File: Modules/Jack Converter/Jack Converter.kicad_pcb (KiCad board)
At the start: 2 copper layers, 45 x 175 mm, 27 parts, among them J1 TS_Jack_3.5mm_Sw, J10 TS_Jack_6.35mm_Sw, J100 IDC_02x08, J11 TS_Jack_3.5mm_Sw, J12 TS_Jack_6.35mm_Sw, J13 TS_Jack_3.5mm_Sw, J14 TS_Jack_6.35mm_Sw, J15 TS_Jack_3.5mm_Sw, J16 TS_Jack_6.35mm_Sw, J17 TS_Jack_3.5mm_Sw, J18 TS_Jack_6.35mm_Sw, J2 TS_Jack_6.35mm_Sw, J3 TS_Jack_3.5mm_Sw, J4 TS_Jack_6.35mm_Sw, J5 TS_Jack_3.5mm_Sw, J50 Conn_01x08_BackboneTap, J6 TS_Jack_6.35mm_Sw, J7 TS_Jack_3.5mm_Sw, J8 TS_Jack_6.35mm_Sw, J9 TS_Jack_3.5mm_Sw, SW1 SW_DPDT, SW2 SW_DPDT, SW3 SW_DPDT

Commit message: Positioned components precisely
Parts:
- moved J17 8.94 mm to (72.5, 185.0), turned to 90 degrees
- moved J18 8.54 mm to (89.0, 185.0), turned to 90 degrees
- moved J100 8.51 mm to (53.2, 186.1)
- moved J15 8.06 mm to (72.5, 168.5), turned to 90 degrees
- moved J16 7.51 mm to (89.0, 168.5), turned to 90 degrees
- moved J13 7.21 mm to (72.5, 152.0), turned to 90 degrees
- moved J14 6.74 mm to (89.0, 152.0), turned to 90 degrees
- moved TP4 6.58 mm to (56.0, 152.0)
- moved J11 6.40 mm to (72.5, 135.5), turned to 90 degrees
- moved J50 6.21 mm to (63.6, 215.0)
- moved J9 6.02 mm to (72.5, 119.0), turned to 90 degrees
- moved J12 5.98 mm to (89.0, 135.5), turned to 90 degrees
- moved J10 5.26 mm to (89.0, 119.0), turned to 90 degrees
- moved TP3 5.10 mm to (56.0, 119.0)
- moved SW3 5.08 mm to (54.7, 133.0)
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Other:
- board size 45 x 175 mm -> 48 x 175 mm

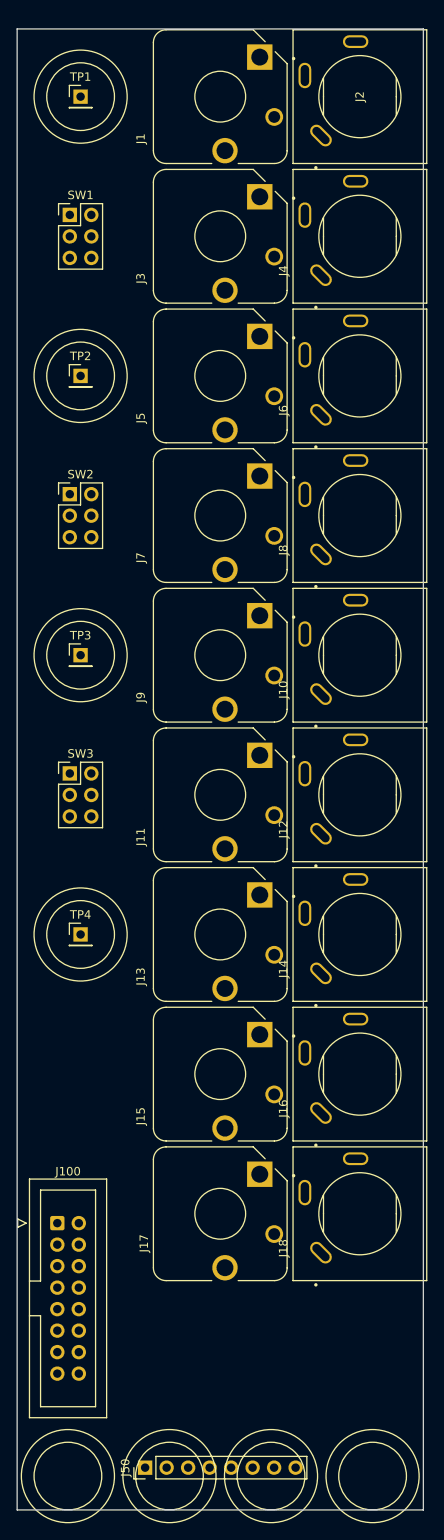
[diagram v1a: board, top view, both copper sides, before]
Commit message: Added extra row of jacks, finished positioning
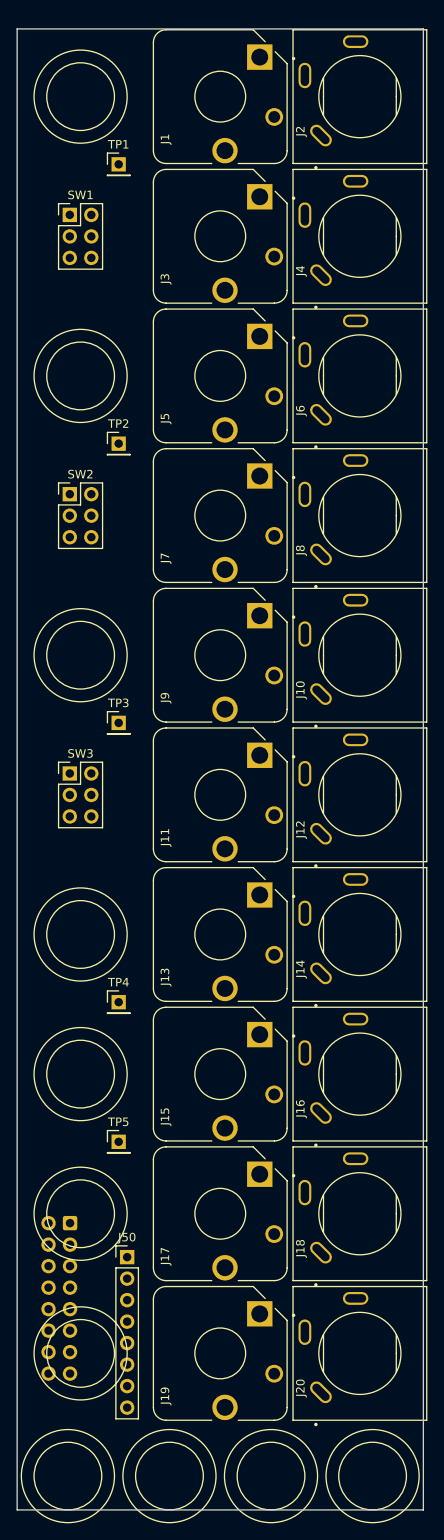
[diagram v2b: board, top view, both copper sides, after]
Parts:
- added J19: TS_Jack_3.5mm_Sw, SynthStuff:AMPHENOL_ACJM-MV35-2S, F.Cu at (72.5, 201.5)
- added J20: TS_Jack_6.35mm_Sw, SynthStuff:CUI_MJ-63052A, F.Cu at (89.0, 201.5)
- added TP5: Banana_Jack, Connector_PinHeader_2.54mm:PinHeader_1x01_P2.54mm_Vertical, F.Cu at (60.5, 176.5)
- J100: moved to B.Cu
- moved J50 25.0 mm to (61.5, 190.1), turned to 0 degrees
- moved TP1 9.18 mm to (60.5, 61.0)
- moved TP2 9.18 mm to (60.5, 94.0)
- moved TP3 9.18 mm to (60.5, 127.0)
- moved TP4 9.18 mm to (60.5, 160.0)
- moved J100 1.50 mm to (54.8, 186.1), turned to 180 degrees
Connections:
- J15 pad T: Net-(J100-Pin_7a) -> Net-(J15-PadT)
- J16 pad T: Net-(J100-Pin_7a) -> Net-(J15-PadT)
- J17 pad T: Net-(J100-Pin_8a) -> Net-(J100-Pin_7a)
- J18 pad T: Net-(J100-Pin_8a) -> Net-(J100-Pin_7a)

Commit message: Routed tracks
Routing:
- net GND: track 0.00 -> 262.3 mm
- net Net-(J10-PadT): track 0.00 -> 82.9 mm
- net Net-(J5-PadT): track 0.00 -> 82.7 mm
- net Net-(J13-PadT): track 0.00 -> 66.2 mm
- net Net-(J1-PadT): track 0.00 -> 51.9 mm
- net Net-(J100-Pin_7a): track 0.00 -> 51.7 mm
- net Net-(J100-Pin_8a): track 0.00 -> 44.5 mm
- net Net-(J11-PadT): track 0.00 -> 40.4 mm
- net Net-(J7-PadT): track 0.00 -> 40.4 mm
- net Net-(J3-PadT): track 0.00 -> 40.4 mm
- net Net-(J15-PadT): track 0.00 -> 35.2 mm
- net -12V: track 0.00 -> 11.0 mm
- net +5V: track 0.00 -> 11.0 mm
- net +12V: track 0.00 -> 11.0 mm

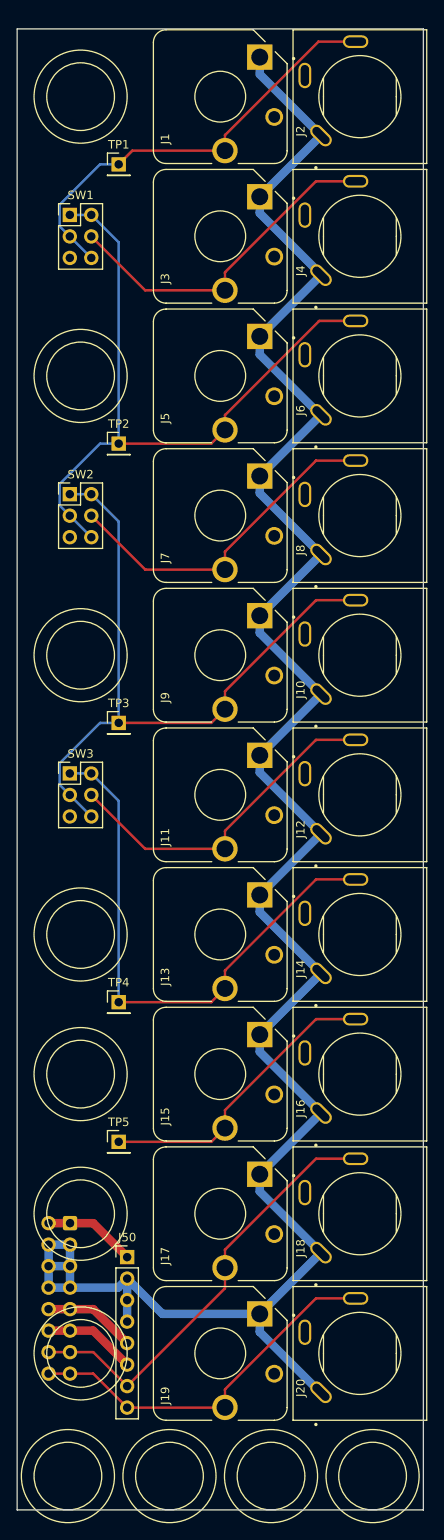
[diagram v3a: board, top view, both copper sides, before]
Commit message: Added GND plane and space for switches
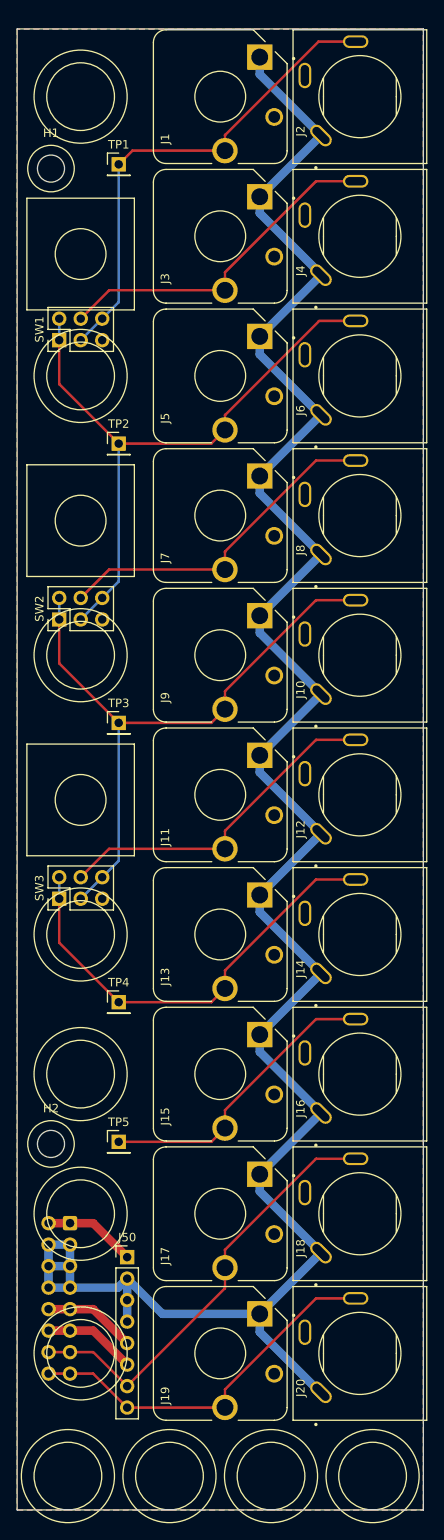
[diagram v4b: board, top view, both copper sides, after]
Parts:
- added H1: MountingHole, MountingHole:MountingHole_3.2mm_M3, F.Cu at (52.5, 61.5)
- added H2: MountingHole, MountingHole:MountingHole_3.2mm_M3, F.Cu at (52.5, 176.8)
- moved SW1 14.9 mm to (53.5, 81.8), turned to 90 degrees
- moved SW2 14.9 mm to (53.5, 114.8), turned to 90 degrees
- moved SW3 14.9 mm to (53.5, 147.8), turned to 90 degrees
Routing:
- net Net-(J13-PadT): track 66.2 -> 52.9 mm
- net Net-(J10-PadT): track 82.9 -> 75.6 mm
- net Net-(J5-PadT): track 82.7 -> 76.0 mm
- net Net-(J1-PadT): track 51.9 -> 57.7 mm
- added copper zone on B.Cu, net GND
- added copper zone on F.Cu, net GND

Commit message: Sent banana jack and switch pinheaders to the back
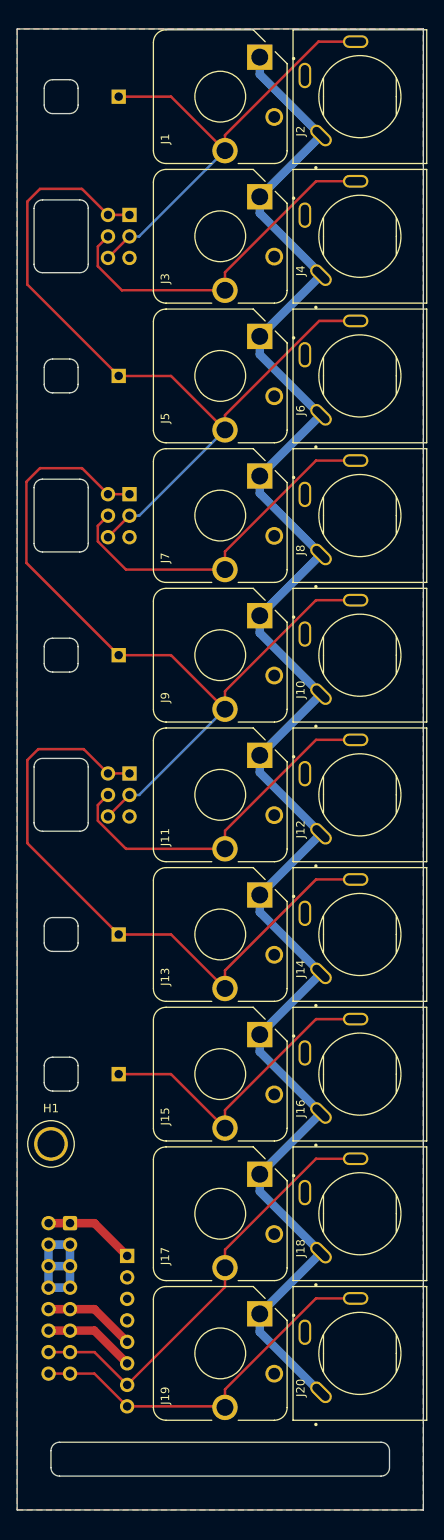
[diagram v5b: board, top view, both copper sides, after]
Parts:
- removed H2: MountingHole, MountingHole:MountingHole_3.2mm_M3
- H1: value MountingHole -> MountingHole_Pad; footprint MountingHole:MountingHole_3.2mm_M3 -> SynthStuff:MountingHole_3.2mm_M3_Pad4mm
- J50, SW1, SW2, SW3, TP1, TP2, TP3, TP4, TP5: moved to B.Cu
- moved H1 115.2 mm to (52.5, 176.8)
- moved SW1 17.0 mm to (61.8, 67.0), turned to 180 degrees
- moved SW2 17.0 mm to (61.8, 100.0), turned to 180 degrees
- moved SW3 17.0 mm to (61.8, 133.0), turned to 180 degrees
- moved TP1 8.00 mm to (60.5, 53.0), turned to 180 degrees
- moved TP2 8.00 mm to (60.5, 86.0), turned to 180 degrees
- moved TP3 8.00 mm to (60.5, 119.0), turned to 180 degrees
- moved TP4 8.00 mm to (60.5, 152.0), turned to 180 degrees
- moved TP5 8.00 mm to (60.5, 168.5), turned to 180 degrees
- moved J50 0.15 mm to (61.5, 190.0), turned to 180 degrees
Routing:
- net GND: track 262.3 -> 232.6 mm
- net Net-(J13-PadT): track 52.9 -> 76.1 mm
- net Net-(J10-PadT): track 75.6 -> 95.4 mm
- net Net-(J5-PadT): track 76.0 -> 95.1 mm
- net Net-(J15-PadT): track 35.2 -> 37.2 mm
- net Net-(J3-PadT): track 40.5 -> 42.2 mm
- net Net-(J1-PadT): track 57.7 -> 56.1 mm
- net Net-(J11-PadT): track 40.5 -> 42.0 mm
- net Net-(J7-PadT): track 40.5 -> 42.0 mm
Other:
- outline, holes or cut-outs redrawn

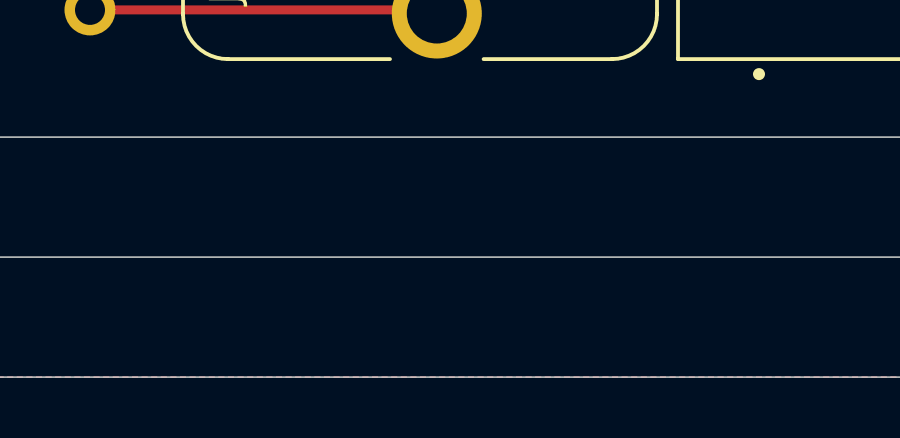
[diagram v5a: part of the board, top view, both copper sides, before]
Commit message: Added board name and serial number placeholder
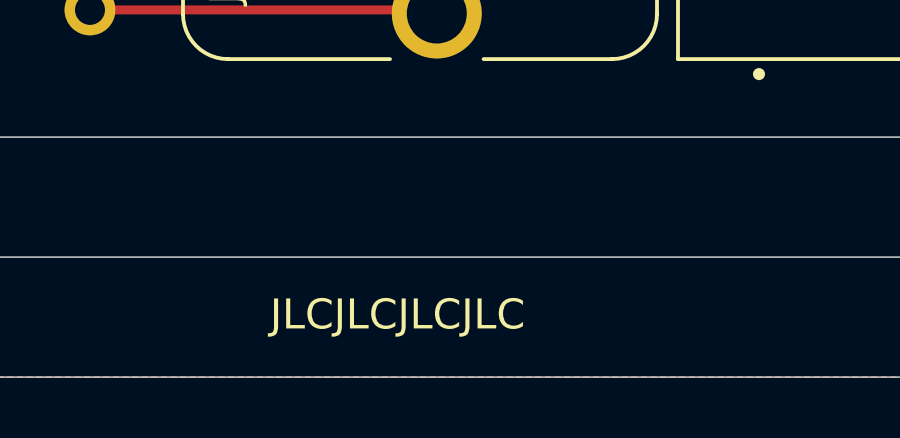
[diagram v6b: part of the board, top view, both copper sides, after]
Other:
- board text added: "JLCJLCJLCJLC"
- board text added: "Jack Converter Mk1 - May 2024"
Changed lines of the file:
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@@
 		)
 		(fp_text user "${REFERENCE}"
-			(at 0 -8.89 270)
+			(at 0 -8.89 -90)
 			(layer "B.Fab")
 			(effects
@@
 		(tags "Through hole vertical IDC box header THT 2x08 2.54mm double row")
 		(property "Reference" "J100"
-			(at 1.27 6.1 180)
+			(at -1.7475 6.11 180)
 			(layer "B.SilkS")
 			(effects
@@
 		(layer "User.9")
 	)
+	(gr_text "Jack Converter Mk1 - May 2024"
+		(at 85 218.5 0)
+		(layer "B.SilkS")
+		(effects
+			(font
+				(size 1 1)
+				(thickness 0.1)
+			)
+			(justify left bottom mirror)
+		)
+	)
+	(gr_text "JLCJLCJLCJLC"
+		(at 67.5 218.5 0)
+		(layer "F.SilkS")
+		(effects
+			(font
+				(size 1 1)
+				(thickness 0.1)
+			)
+			(justify left bottom)
+		)
+	)
 	(segment

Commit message: Removed spacer hole and updated sheets
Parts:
- removed H1: MountingHole_Pad, SynthStuff:MountingHole_3.2mm_M3_Pad4mm
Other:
- board text added: "Adapter Mult Mk1 - May 2024"
- board text removed: "Jack Converter Mk1 - May 2024"
